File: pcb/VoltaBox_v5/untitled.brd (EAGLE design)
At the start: 100 x 80 mm, 58 parts, among them J1 1050170001, X1 112J-TDAR-R(MICROSD), X2 52892-0895, X3 52892-0895, X4 292304-3

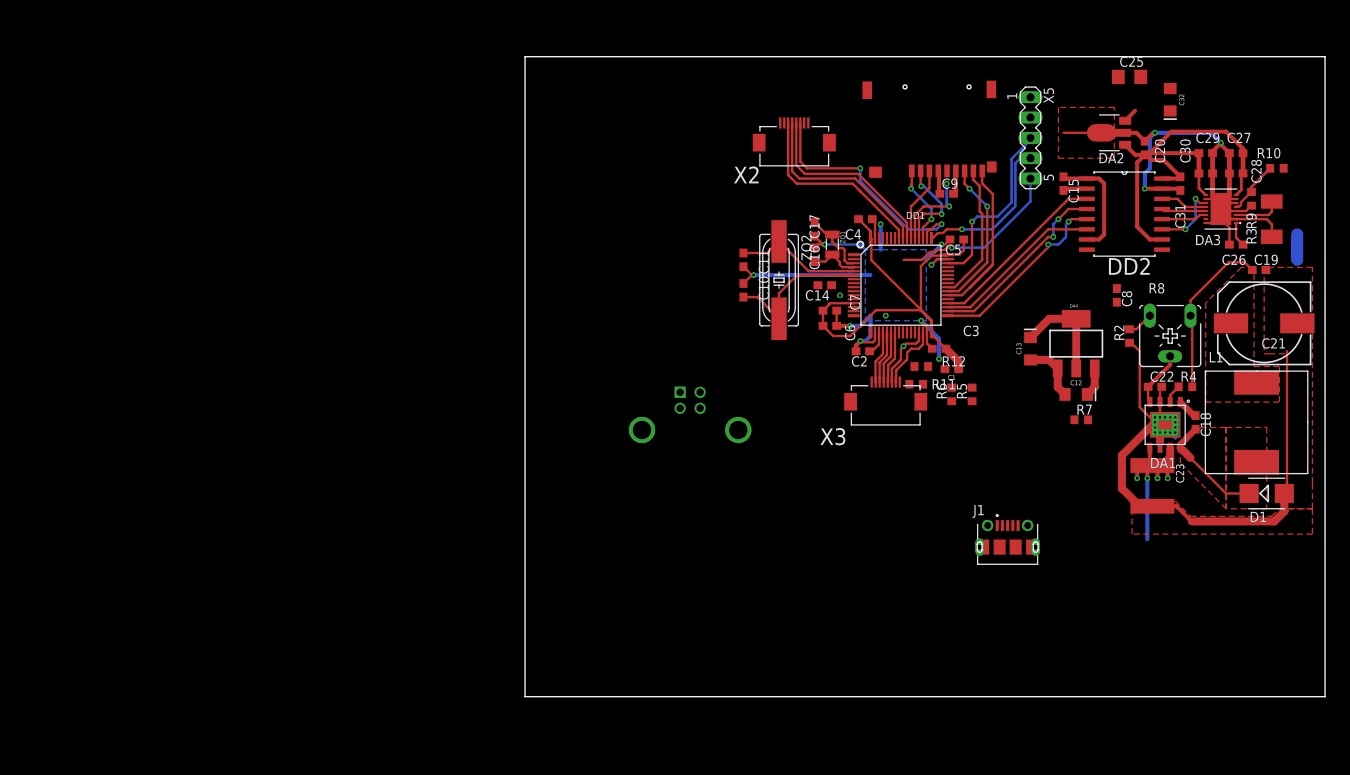
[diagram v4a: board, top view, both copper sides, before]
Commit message: usb route done, some pcb and schematic changes, added power connectors, dc-dc diode replaced, added TODO file
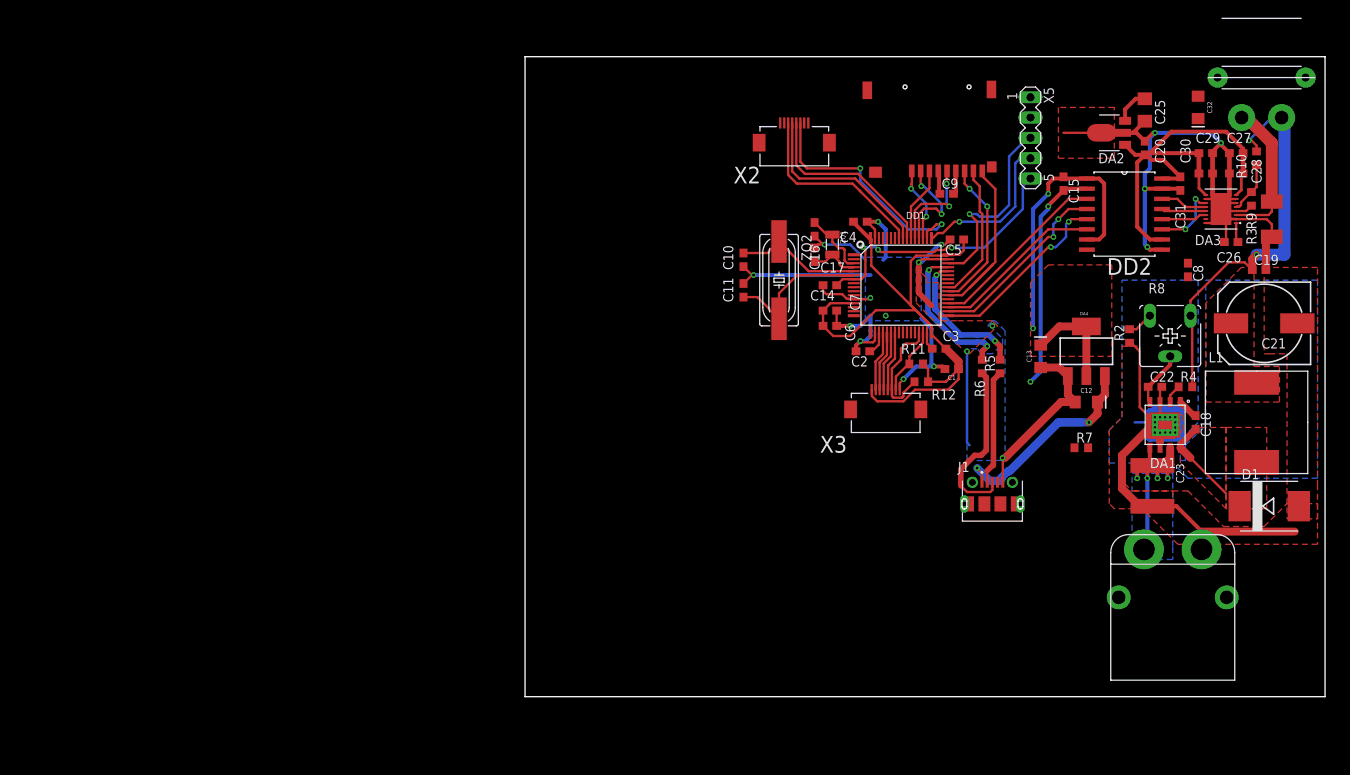
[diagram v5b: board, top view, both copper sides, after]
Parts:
- added X6: XT60PW-M, untitled:XT60PW-M
- D1: value STPS3L60U -> STPS5L60S; device untitled:SMB -> untitled:SMC
- X4: value 292304-3 -> XT30PW-F; device 292304-3:TE_292304-3 -> untitled:XT30PW-F
- moved X4 81.4 mm to (92.1, 72.4), flipped to the top
- moved C8 9.44 mm to (82.9, 53.3)
- moved J1 5.72 mm to (58.4, 24.4)
- moved R6 5.17 mm to (57.1, 41.3)
- moved R5 4.94 mm to (59.4, 41.3)
- moved C25 4.55 mm to (77.5, 73.3), turned to 270 degrees
- moved C32 3.62 mm to (84.1, 73.7)
- moved R7 3.49 mm to (69.5, 31.1)
- moved R10 2.84 mm to (91.4, 67.3), turned to 90 degrees
- moved R11 2.54 mm to (48.9, 41.6)
- moved R12 1.91 mm to (49.5, 39.4)
- moved D1 1.62 mm to (93.0, 23.8)
- moved C12 1.59 mm to (70.2, 36.8)
- moved DA4 1.59 mm to (70.2, 43.2)
- moved C13 1.59 mm to (64.5, 42.5)
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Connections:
- net N$20 renamed DMCU_P
- net N$21 renamed DMCU_N
- removed net DM: R5.1, X4.2
- removed net DP: R6.1, R7.1, X4.3
- new net D_N: J1.2, R5.1
- new net D_P: J1.3, R6.1, R7.1
- net +12V: now also X6.P$2, X6.P$3, X6.P$4
- net +4V: now also X4.P$2, X4.P$3, X4.P$4
- net GND: now also J1.5, J1.SH1, J1.SH2, J1.SH3, J1.SH4, J1.SH5, J1.SH6, J1.SH7, J1.SH8, X6.P$1; no longer X4.4, X4.SH1, X4.SH2
- net N$23: now also X4.P$1
- net VCC: now also J1.1; no longer X4.1
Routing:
- net GND: track 213.5 -> 322.1 mm, vias 14 -> 20
- net +3V3: track 96.7 -> 140.9 mm, vias 0 -> 2
- net VCC: track 3.63 -> 37.9 mm, vias 0 -> 2
- net +4V: track 24.1 -> 51.3 mm, vias 0 -> 2
- net D_P: track 0.00 -> 21.7 mm
- net DMCU_P: track 0.00 -> 19.0 mm, vias 0 -> 2
- net DMCU_N: track 0.00 -> 17.7 mm, vias 0 -> 2
- net D_N: track 0.00 -> 14.2 mm
- net NRESET: track 21.8 -> 34.4 mm, vias 1 -> 3
- net N$23: track 6.31 -> 18.7 mm
- net N$27: track 8.35 -> 14.1 mm, vias 1 -> 0
- net N$9: track 16.3 -> 13.0 mm
- net +12V: track 23.4 -> 26.1 mm
- net N$14: track 10.6 -> 12.8 mm
- net SWDIO: track 22.5 -> 24.6 mm
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- added copper zone on layer 16, net +12V
- added copper zone on layer 1, net +3V3

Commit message: pcb adaptation for existing case
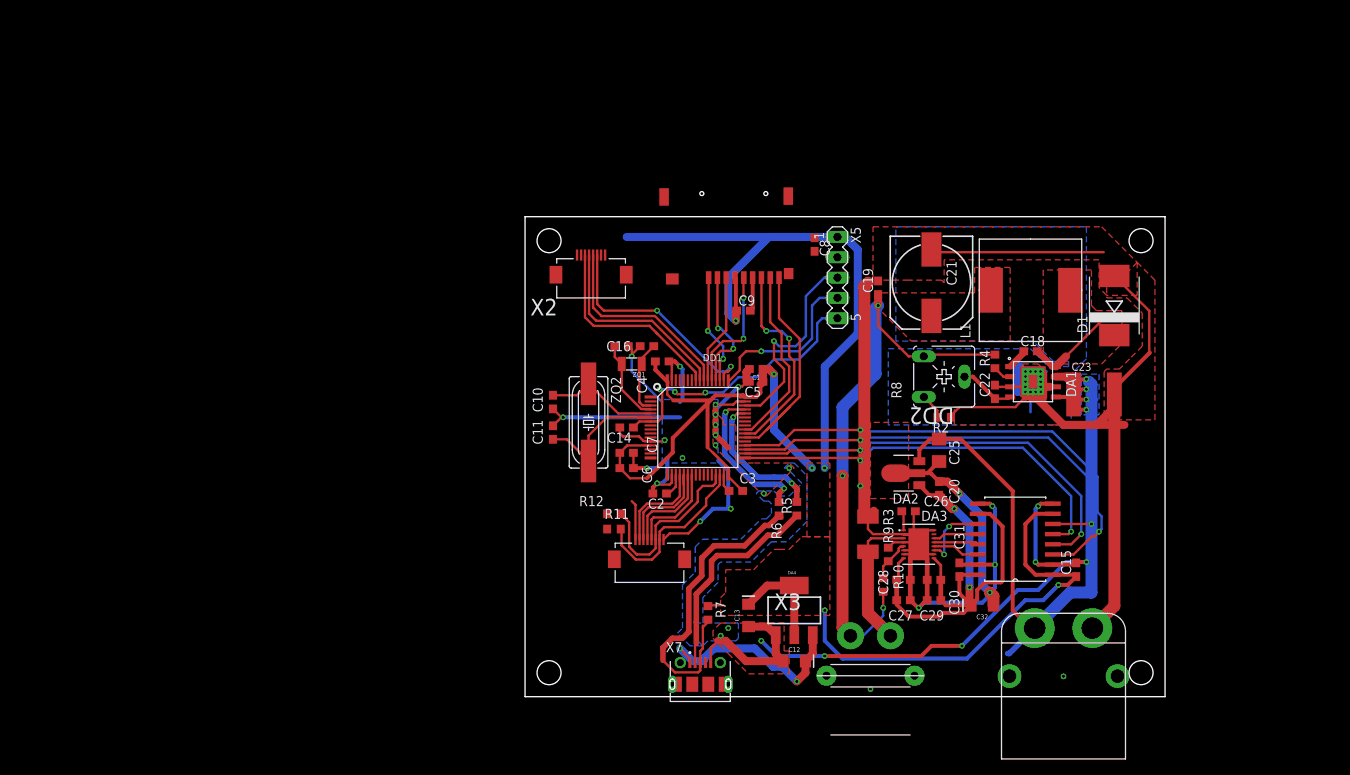
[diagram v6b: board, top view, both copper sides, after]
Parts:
- removed J1: 1050170001, 1050170001:MOLEX_1050170001
- added X7: 1050170001, 1050170001:MOLEX_1050170001
- moved X4 81.2 mm to (43.2, 7.62), turned to 180 degrees
- moved R10 70.9 mm to (44.8, 14.0), turned to 270 degrees
- moved C27 69.7 mm to (47.3, 12.1), turned to 0 degrees
- moved C32 67.8 mm to (57.1, 11.4), turned to 180 degrees
- moved C28 65.7 mm to (47.3, 14.6), turned to 0 degrees
- moved C29 65.4 mm to (51.1, 12.1), turned to 180 degrees
- moved R3 64.0 mm to (42.9, 20.3), turned to 270 degrees
- moved R9 63.5 mm to (45.4, 17.8), turned to 270 degrees
- moved C30 61.1 mm to (51.1, 14.6), turned to 180 degrees
- moved DA3 56.4 mm to (49.2, 19.1), turned to 0 degrees
- moved C31 55.6 mm to (54.3, 15.9), turned to 90 degrees
- moved C26 52.5 mm to (47.9, 23.2), turned to 0 degrees
- moved R7 51.0 mm to (22.9, 10.5), turned to 90 degrees
- moved DA2 49.7 mm to (47.3, 27.9)
- moved C20 49.7 mm to (51.8, 26.0)
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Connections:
- net D_N: now also X7.2; no longer J1.2
- net D_P: now also X7.3; no longer J1.3
- net GND: now also X7.5, X7.SH1, X7.SH2, X7.SH3, X7.SH4, X7.SH5, X7.SH6, X7.SH7, X7.SH8; no longer J1.5, J1.SH1, J1.SH2, J1.SH3, J1.SH4, J1.SH5, J1.SH6, J1.SH7, J1.SH8
- net VCC: now also X7.1; no longer J1.1
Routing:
- net GND: track 322.1 -> 429.7 mm, vias 20 -> 31
- net +3V3: track 140.9 -> 242.5 mm, vias 2 -> 6
- net +12V: track 26.1 -> 90.3 mm
- net ADC_MOSI: track 22.7 -> 61.5 mm, vias 0 -> 2
- net ADC_MISO: track 21.4 -> 56.4 mm, vias 0 -> 2
- net ADC_SCK: track 23.6 -> 54.2 mm
- net ADC_NSS: track 23.3 -> 50.9 mm
- net +4V: track 51.3 -> 71.8 mm, vias 2 -> 3
- net D_P: track 21.7 -> 40.0 mm
- net N$24: track 8.63 -> 22.3 mm
- net D_N: track 14.2 -> 26.5 mm
- net +5V: track 56.7 -> 68.6 mm, vias 0 -> 2
- net VCC: track 37.9 -> 26.7 mm
- net N$27: track 14.1 -> 23.0 mm
- net N$19: track 19.4 -> 26.0 mm
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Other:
- board size 100 x 80 mm -> 80 x 60 mm

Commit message: pre final
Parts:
- added J1: 0, rcl:R2010
- X7: value 1050170001 -> KLS1-233; device 1050170001:MOLEX_1050170001 -> untitled:KLS1-233
- moved R5 12.8 mm to (24.1, 15.2), turned to 0 degrees
- moved R6 9.72 mm to (24.1, 17.5), turned to 0 degrees
- moved R11 6.61 mm to (5.71, 17.1)
- moved R12 6.61 mm to (5.71, 19.1)
- moved X3 6.61 mm to (10.2, 18.7)
- moved X1 5.08 mm to (31.8, 47.3)
- moved C9 4.45 mm to (27.3, 43.8)
- moved C3 4.02 mm to (25.1, 21.9)
- moved DA4 3.81 mm to (29.8, 10.8)
- moved C12 3.49 mm to (30.2, 4.45)
- moved C15 3.49 mm to (68.9, 19.4)
- moved DD2 3.49 mm to (61.3, 23.2)
- moved C1 3.19 mm to (29.2, 37.8)
- moved C11 3.19 mm to (3.17, 29.8)
- moved C25 3.19 mm to (54.9, 31.1)
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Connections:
- net +12V: now also J1.1; no longer X6.P$3, X6.P$4
- net +4V: now also J1.2; no longer X4.P$3, X4.P$4
- net GND: no longer X7.SH1, X7.SH2, X7.SH3, X7.SH8
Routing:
- net +3V3: track 242.5 -> 344.7 mm, vias 6 -> 8
- net GND: track 429.7 -> 488.2 mm, vias 31 -> 28
- net OLED_DC: track 0.00 -> 28.0 mm
- net +4V: track 71.8 -> 89.3 mm, vias 3 -> 4
- net D_P: track 40.0 -> 30.3 mm
- net D_N: track 26.5 -> 17.2 mm
- net DMCU_N: track 17.7 -> 24.0 mm
- net N$28: track 11.8 -> 17.9 mm
- net N$30: track 13.3 -> 19.2 mm
- net N$29: track 11.9 -> 17.7 mm
- net N$27: track 23.0 -> 28.5 mm
- net N$31: track 12.1 -> 17.3 mm
- net N$24: track 22.3 -> 27.4 mm
- net N$32: track 29.0 -> 24.1 mm
- net ADC_MISO: track 56.4 -> 51.7 mm
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
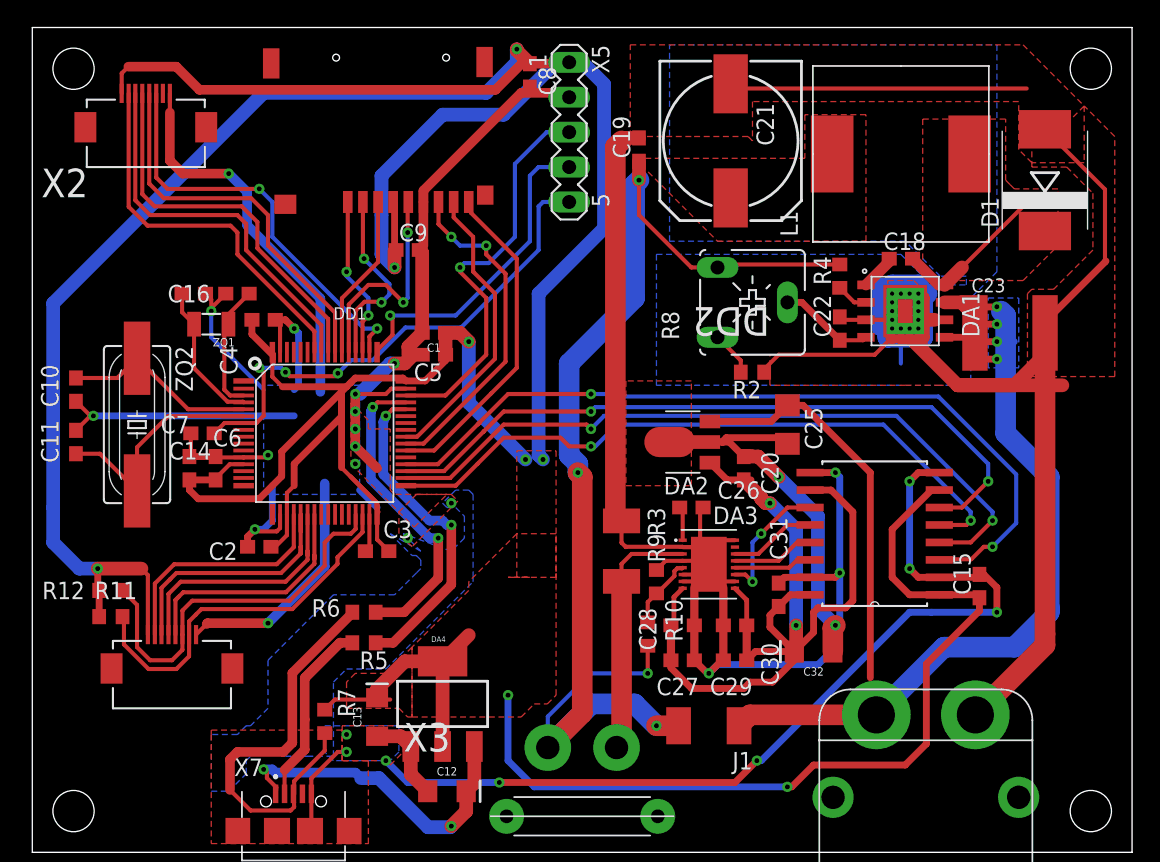
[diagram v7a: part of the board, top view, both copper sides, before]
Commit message: Put some silk to the it's places. Added 3 testpoints.
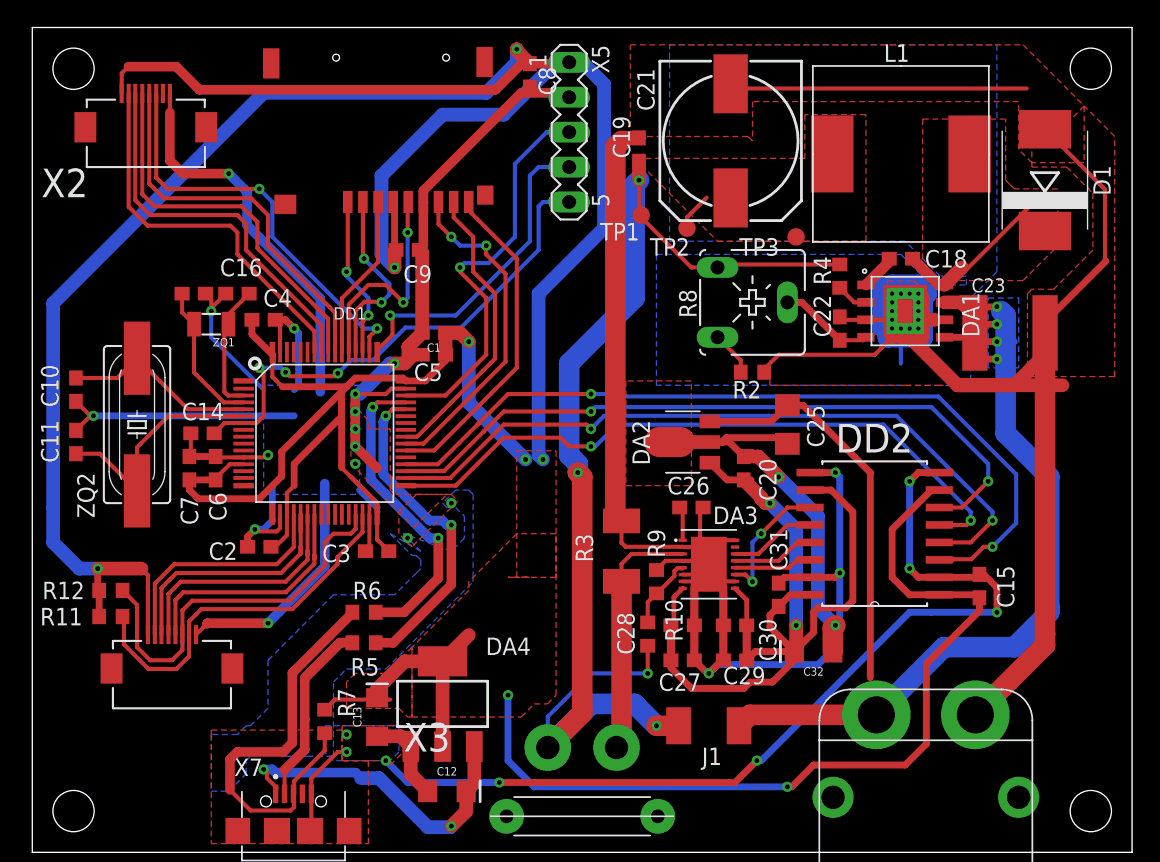
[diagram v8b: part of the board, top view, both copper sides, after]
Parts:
- added TP1, TP2, TP3: TPSQB1,27, testpad:B1,27
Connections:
- net +4V: now also TP1.TP, TP2.TP, TP3.TP
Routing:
- net +4V: track 89.3 -> 92.1 mm
